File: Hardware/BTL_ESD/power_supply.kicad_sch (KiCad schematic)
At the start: 46 parts, among them J2 DC-005-5A-2.0, U1 AMS1117-3.3, U6 ICL7662CBA-T, U7 TPS54331D

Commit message: hardware: ver 1 schematic
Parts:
- added SW1: MS-22D18G2ROHS, MS-22D18G2ROHS:SW_MS-22D18G2ROHS, symbol MS-22D18G2ROHS:MS-22D18G2ROHS
- renumbered C12 to C1, C5 to C10, C15 to C11, C16 to C12, C7 to C13, C8 to C14, C9 to C15, C10 to C16, C1 to C2, C2 to C3, C13 to C4, C3 to C5, C4 to C6, C14 to C7, C11 to C8, C6 to C9, J2 to J1, R6 to R10, R7 to R4, R8 to R5, R9 to R6, R10 to R7, R4 to R8, R5 to R9, U6 to U1, U1 to U2, U7 to U3
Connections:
- net +5V: now also SW1.5; no longer C15.1, C16.1, L1.2, R8.1
- new net V_USB: SW1.4
- new net Vin: C15.1, C16.1, L1.2, R8.1, SW1.6
- no-connect marks 2 -> 5
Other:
- note added: "SELECT SUPPLY"
- moved on the sheet: C1, C11, C12, C4, C7, C8, D3, D4, D5, D6, H1, H2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

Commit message: update
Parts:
- added NT1: NetTie_2, NetTie:NetTie-2_SMD_Pad2.0mm, symbol Device:NetTie_2
- added NT2: NetTie_2, NetTie:NetTie-2_SMD_Pad0.5mm, symbol Device:NetTie_2
- C15, C16: footprint Capacitor_SMD:C_0603_1608Metric_Pad1.08x0.95mm_HandSolder -> Capacitor_SMD:C_0805_2012Metric_Pad1.18x1.45mm_HandSolder; URL https://www.thegioiic.com/tu-gom-0603-47uf-6-3v -> https://www.thegioiic.com/tu-gom-0805-47uf-6-3v
- C3, C5: value 4.7uF/25V -> 4.7uF/50V; footprint Capacitor_SMD:C_0603_1608Metric_Pad1.08x0.95mm_HandSolder -> Capacitor_SMD:C_0805_2012Metric_Pad1.18x1.45mm_HandSolder; URL https://www.thegioiic.com/tu-gom-0603-4-7uf-25v -> https://www.thegioiic.com/tu-gom-0805-4-7uf-50v
- C6: value 4.7uF/25V -> 10pF/50V; footprint Capacitor_SMD:C_0603_1608Metric_Pad1.08x0.95mm_HandSolder -> Capacitor_SMD:C_0805_2012Metric_Pad1.18x1.45mm_HandSolder; URL https://www.thegioiic.com/tu-gom-0603-4-7uf-25v -> https://www.thegioiic.com/tu-gom-0805-10pf-50v
- D2: value SS34 -> SS54; URL https://www.thegioiic.com/twgmc-ss34-sma-diode-schottky-3a -> https://www.thegioiic.com/ss54-sma-diode-shotky-5a-40v
- L1: value 6.8uH/2.2A -> 6.8uH/4.4A; footprint Inductor_SMD:L_Cenker_CKCS5040 -> L8D43:CDRH8D43NP-6R8; URL https://www.thegioiic.com/cuon-cam-dan-smd-cd53-5852-6r8-6-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 -> http://www.tme.vn/Product.aspx?id=1383#page=pro_info
- R3: value 33k/1% -> 30k/1%
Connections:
- net +5V: now also SW1.2
- net GND: now also NT1.1, NT2.1
- net V_USB: now also SW1.3
- net Vin: now also SW1.1
- new net GND1: NT2.2
- new net GNDA: NT1.2
- no-connect marks 5 -> 2

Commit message: fea:STM32: upload structure fodler
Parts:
- removed H4: BoreHole, MountingHole:MountingHole_3.2mm_M3_Pad_TopBottom, symbol Mechanical:MountingHole
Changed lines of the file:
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@@
-    )
-  )
-  (symbol (lib_id "Mechanical:MountingHole") (at 161.29 146.05 0) (unit 1)
-    (in_bom yes) (on_board yes) (dnp no) (fields_autoplaced)
-    (property "Reference" "H4" (at 163.83 144.78 0)
-      (effects (font (size 1.27 1.27)) (justify left))
-    )
-    (property "Value" "BoreHole" (at 163.83 147.32 0)
-      (effects (font (size 1.27 1.27)) (justify left))
-    )
-    (property "Footprint" "MountingHole:MountingHole_3.2mm_M3_Pad_TopBottom" (at 161.29 146.05 0)
-      (effects (font (size 1.27 1.27)) hide)
-    )
-    (property "Datasheet" "~" (at 161.29 146.05 0)
-      (effects (font (size 1.27 1.27)) hide)
-    )
-    (instances
-      (project "BTL_ESD"
-        (path "/ce4779b4-6d78-42e3-84df-0a4e77629b0f/fb6de343-a930-422d-a1ac-a921f45011d1"
-          (reference "H4") (unit 1)
-        )
-      )
     )
   )

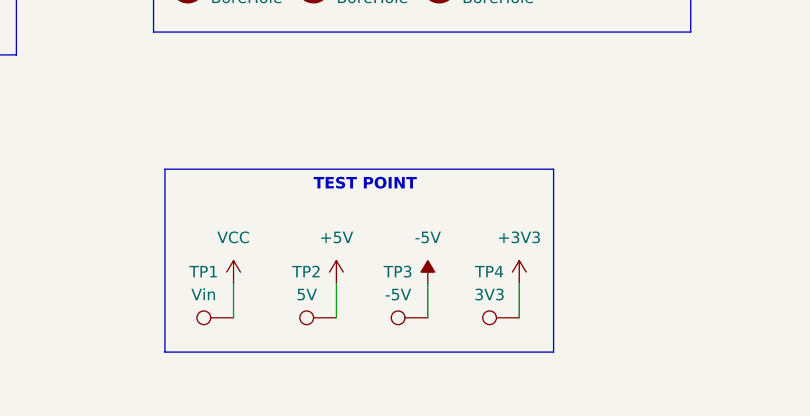
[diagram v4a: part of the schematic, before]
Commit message: hardware:update pcb track power
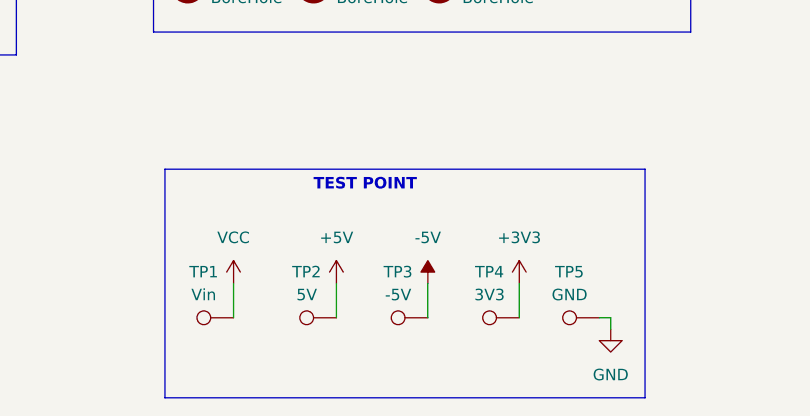
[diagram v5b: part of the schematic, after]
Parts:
- added TP5: GND, TestPoint:TestPoint_Pad_D2.5mm, symbol Connector:TestPoint
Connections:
- net GND: now also TP5.1
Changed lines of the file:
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@@
+    (stroke (width 0) (type default))
+  )
+  (wire (pts (xy 166.37 182.88) (xy 165.1 182.88))
     (stroke (width 0) (type default))
   )
@@
     (stroke (width 0) (type default))
   )
+  (wire (pts (xy 166.37 184.15) (xy 166.37 182.88))
+    (stroke (width 0) (type default))
+  )
   (wire (pts (xy 100.33 62.23) (xy 115.57 62.23))
     (stroke (width 0) (type default))
@@
     (fill (type none))
   )
-  (rectangle (start 116.84 166.37) (end 160.02 186.69)
+  (rectangle (start 116.84 166.37) (end 170.18 191.77)
     (stroke (width 0) (type default))
     (fill (type none))
@@
   (symbol (lib_id "power:GND") (at 245.11 134.62 0) (unit 1)
     (in_bom yes) (on_board yes) (dnp no) (fields_autoplaced)
-    (property "Reference" "#PWR025" (at 245.11 140.97 0)
+    (property "Reference" "#PWR026" (at 245.11 140.97 0)
       (effects (font (size 1.27 1.27)) hide)
     )
@@
       (project "BTL_ESD"
         (path "/ce4779b4-6d78-42e3-84df-0a4e77629b0f/fb6de343-a930-422d-a1ac-a921f45011d1"
-          (reference "#PWR025") (unit 1)
+          (reference "#PWR026") (unit 1)
         )
       )
@@
   (symbol (lib_id "power:GND") (at 209.55 152.4 0) (unit 1)
     (in_bom yes) (on_board yes) (dnp no) (fields_autoplaced)
-    (property "Reference" "#PWR017" (at 209.55 158.75 0)
+    (property "Reference" "#PWR018" (at 209.55 158.75 0)
       (effects (font (size 1.27 1.27)) hide)
     )
@@
       (project "BTL_ESD"
         (path "/ce4779b4-6d78-42e3-84df-0a4e77629b0f/fb6de343-a930-422d-a1ac-a921f45011d1"
-          (reference "#PWR017") (unit 1)
+          (reference "#PWR018") (unit 1)
         )
       )
@@
     )
   )
+  (symbol (lib_id "Connector:TestPoint") (at 165.1 182.88 90) (unit 1)
+    (in_bom yes) (on_board yes) (dnp no) (fields_autoplaced)
+    (property "Reference" "TP5" (at 161.798 177.8 90)
+      (effects (font (size 1.27 1.27)))
+    )
+    (property "Value" "GND" (at 161.798 180.34 90)
+      (effects (font (size 1.27 1.27)))
+    )
+    (property "Footprint" "TestPoint:TestPoint_Pad_D2.5mm" (at 165.1 177.8 0)
+      (effects (font (size 1.27 1.27)) hide)
+    )
+    (property "Datasheet" "~" (at 165.1 177.8 0)
+      (effects (font (size 1.27 1.27)) hide)
+    )
+    (pin "1")
+    (instances
+      (project "BTL_ESD"
+        (path "/ce4779b4-6d78-42e3-84df-0a4e77629b0f/fb6de343-a930-422d-a1ac-a921f45011d1"
+          (reference "TP5") (unit 1)
+        )
+      )
+    )
+  )
   (symbol (lib_id "power:-5V") (at 218.44 129.54 0) (unit 1)
     (in_bom yes) (on_board yes) (dnp no) (fields_autoplaced)
-    (property "Reference" "#PWR021" (at 218.44 127 0)
+    (property "Reference" "#PWR022" (at 218.44 127 0)
       (effects (font (size 1.27 1.27)) hide)
     )
@@
       (project "BTL_ESD"
         (path "/ce4779b4-6d78-42e3-84df-0a4e77629b0f/fb6de343-a930-422d-a1ac-a921f45011d1"
-          (reference "#PWR021") (unit 1)
+          (reference "#PWR022") (unit 1)
         )
       )
@@
   (symbol (lib_id "power:VCC") (at 218.44 102.87 0) (unit 1)
     (in_bom yes) (on_board yes) (dnp no) (fields_autoplaced)
-    (property "Reference" "#PWR018" (at 218.44 106.68 0)
+    (property "Reference" "#PWR019" (at 218.44 106.68 0)
       (effects (font (size 1.27 1.27)) hide)
     )
@@
       (project "BTL_ESD"
         (path "/ce4779b4-6d78-42e3-84df-0a4e77629b0f/fb6de343-a930-422d-a1ac-a921f45011d1"
-          (reference "#PWR018") (unit 1)
+          (reference "#PWR019") (unit 1)
         )
       )
@@
   (symbol (lib_id "power:GNDA") (at 243.84 154.94 0) (unit 1)
     (in_bom yes) (on_board yes) (dnp no) (fields_autoplaced)
-    (property "Reference" "#PWR024" (at 243.84 161.29 0)
+    (property "Reference" "#PWR025" (at 243.84 161.29 0)
       (effects (font (size 1.27 1.27)) hide)
     )
@@
       (project "BTL_ESD"
         (path "/ce4779b4-6d78-42e3-84df-0a4e77629b0f/fb6de343-a930-422d-a1ac-a921f45011d1"
-          (reference "#PWR024") (unit 1)
+          (reference "#PWR025") (unit 1)
         )
       )
@@
   (symbol (lib_id "power:+3V3") (at 187.96 101.6 0) (unit 1)
     (in_bom yes) (on_board yes) (dnp no) (fields_autoplaced)
-    (property "Reference" "#PWR016" (at 187.96 105.41 0)
+    (property "Reference" "#PWR017" (at 187.96 105.41 0)
       (effects (font (size 1.27 1.27)) hide)
     )
@@
       (project "BTL_ESD"
         (path "/ce4779b4-6d78-42e3-84df-0a4e77629b0f/fb6de343-a930-422d-a1ac-a921f45011d1"
-          (reference "#PWR016") (unit 1)
+          (reference "#PWR017") (unit 1)
         )
       )
@@
   (symbol (lib_id "power:GND1") (at 236.22 160.02 0) (unit 1)
     (in_bom yes) (on_board yes) (dnp no) (fields_autoplaced)
-    (property "Reference" "#PWR023" (at 236.22 166.37 0)
+    (property "Reference" "#PWR024" (at 236.22 166.37 0)
       (effects (font (size 1.27 1.27)) hide)
     )
@@
       (project "BTL_ESD"
         (path "/ce4779b4-6d78-42e3-84df-0a4e77629b0f/fb6de343-a930-422d-a1ac-a921f45011d1"
-          (reference "#PWR023") (unit 1)
+          (reference "#PWR024") (unit 1)
         )
       )
@@
   (symbol (lib_id "power:+3V3") (at 218.44 111.76 0) (unit 1)
     (in_bom yes) (on_board yes) (dnp no) (fields_autoplaced)
-    (property "Reference" "#PWR019" (at 218.44 115.57 0)
+    (property "Reference" "#PWR020" (at 218.44 115.57 0)
       (effects (font (size 1.27 1.27)) hide)
     )
@@
       (project "BTL_ESD"
         (path "/ce4779b4-6d78-42e3-84df-0a4e77629b0f/fb6de343-a930-422d-a1ac-a921f45011d1"
-          (reference "#PWR019") (unit 1)
+          (reference "#PWR020") (unit 1)
         )
       )
@@
   (symbol (lib_id "power:+5V") (at 218.44 120.65 0) (unit 1)
     (in_bom yes) (on_board yes) (dnp no) (fields_autoplaced)
-    (property "Reference" "#PWR020" (at 218.44 124.46 0)
+    (property "Reference" "#PWR021" (at 218.44 124.46 0)
       (effects (font (size 1.27 1.27)) hide)
     )
@@
       (project "BTL_ESD"
         (path "/ce4779b4-6d78-42e3-84df-0a4e77629b0f/fb6de343-a930-422d-a1ac-a921f45011d1"
-          (reference "#PWR020") (unit 1)
+          (reference "#PWR021") (unit 1)
         )
       )
@@
     )
   )
+  (symbol (lib_id "power:GND") (at 166.37 184.15 0) (unit 1)
+    (in_bom yes) (on_board yes) (dnp no) (fields_autoplaced)
+    (property "Reference" "#PWR016" (at 166.37 190.5 0)
+      (effects (font (size 1.27 1.27)) hide)
+    )
+    (property "Value" "GND" (at 166.37 189.23 0)
+      (effects (font (size 1.27 1.27)))
+    )
+    (property "Footprint" "" (at 166.37 184.15 0)
+      (effects (font (size 1.27 1.27)) hide)
+    )
+    (property "Datasheet" "" (at 166.37 184.15 0)
+      (effects (font (size 1.27 1.27)) hide)
+    )
+    (pin "1")
+    (instances
+      (project "BTL_ESD"
+        (path "/ce4779b4-6d78-42e3-84df-0a4e77629b0f/fb6de343-a930-422d-a1ac-a921f45011d1"
+          (reference "#PWR016") (unit 1)
+        )
+      )
+    )
+  )
   (symbol (lib_id "power:-5V") (at 146.05 179.07 0) (unit 1)
     (in_bom yes) (on_board yes) (dnp no) (fields_autoplaced)
@@
   (symbol (lib_id "power:GND") (at 222.25 76.2 0) (unit 1)
     (in_bom yes) (on_board yes) (dnp no) (fields_autoplaced)
-    (property "Reference" "#PWR022" (at 222.25 82.55 0)
+    (property "Reference" "#PWR023" (at 222.25 82.55 0)
       (effects (font (size 1.27 1.27)) hide)
     )
@@
       (project "BTL_ESD"
         (path "/ce4779b4-6d78-42e3-84df-0a4e77629b0f/fb6de343-a930-422d-a1ac-a921f45011d1"
-          (reference "#PWR022") (unit 1)
-        )
-      )
+          (reference "#PWR023") (unit 1)
+        )
+      )

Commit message: code:ESP32: update uart driver, main.c && hardware file pcb
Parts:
- renumbered TP3 to TP2, TP4 to TP3, TP2 to TP4
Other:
- moved on the sheet: H1, H2, H3, TP2, TP3, TP4, TP5

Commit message: Doc:README:upload frame tranmission
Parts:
- R1: value 330k/1% -> 100k/1%; URL https://www.thegioiic.com/dien-tro-330-kohm-0603-1- -> https://www.thegioiic.com/dien-tro-100-kohm-0603-1-
- R2: value 47k/1% -> 20k/1%; URL https://www.thegioiic.com/dien-tro-47-kohm-0603-1- -> https://www.thegioiic.com/dien-tro-20-kohm-0603-1-
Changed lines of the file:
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@@
       (effects (font (size 1.27 1.27)) (justify left))
     )
-    (property "Value" "47k/1%" (at 133.35 68.58 0)
+    (property "Value" "20k/1%" (at 133.35 68.58 0)
       (effects (font (size 1.27 1.27)) (justify left))
     )
@@
       (effects (font (size 1.27 1.27)) hide)
     )
-    (property "URL" "https://www.thegioiic.com/dien-tro-47-kohm-0603-1-" (at 130.81 67.31 0)
+    (property "URL" "https://www.thegioiic.com/dien-tro-20-kohm-0603-1-" (at 130.81 67.31 0)
       (effects (font (size 1.27 1.27)) hide)
     )
@@
       (effects (font (size 1.27 1.27)) (justify left))
     )
-    (property "Value" "330k/1%" (at 133.35 59.69 0)
+    (property "Value" "100k/1%" (at 133.35 59.69 0)
       (effects (font (size 1.27 1.27)) (justify left))
     )
@@
       (effects (font (size 1.27 1.27)) hide)
     )
-    (property "URL" "https://www.thegioiic.com/dien-tro-330-kohm-0603-1-" (at 130.81 58.42 0)
-      (effects (font (size 1.27 1.27)) hide)
-    )
+    (property "URL" "https://www.thegioiic.com/dien-tro-100-kohm-0603-1-" (at 130.81 58.42 0)
+      (effects (font (size 1.27 1.27)) hide)
+    )
